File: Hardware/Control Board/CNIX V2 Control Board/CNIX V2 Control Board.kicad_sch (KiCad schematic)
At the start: 71 parts, among them J1 EXT, J10 LED, J11 USB_C_Receptacle, J3 Tube Out, J4 EXT, J5 I2C_ext, J6 Prog, J7 HT, J8 GND, J9 GND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

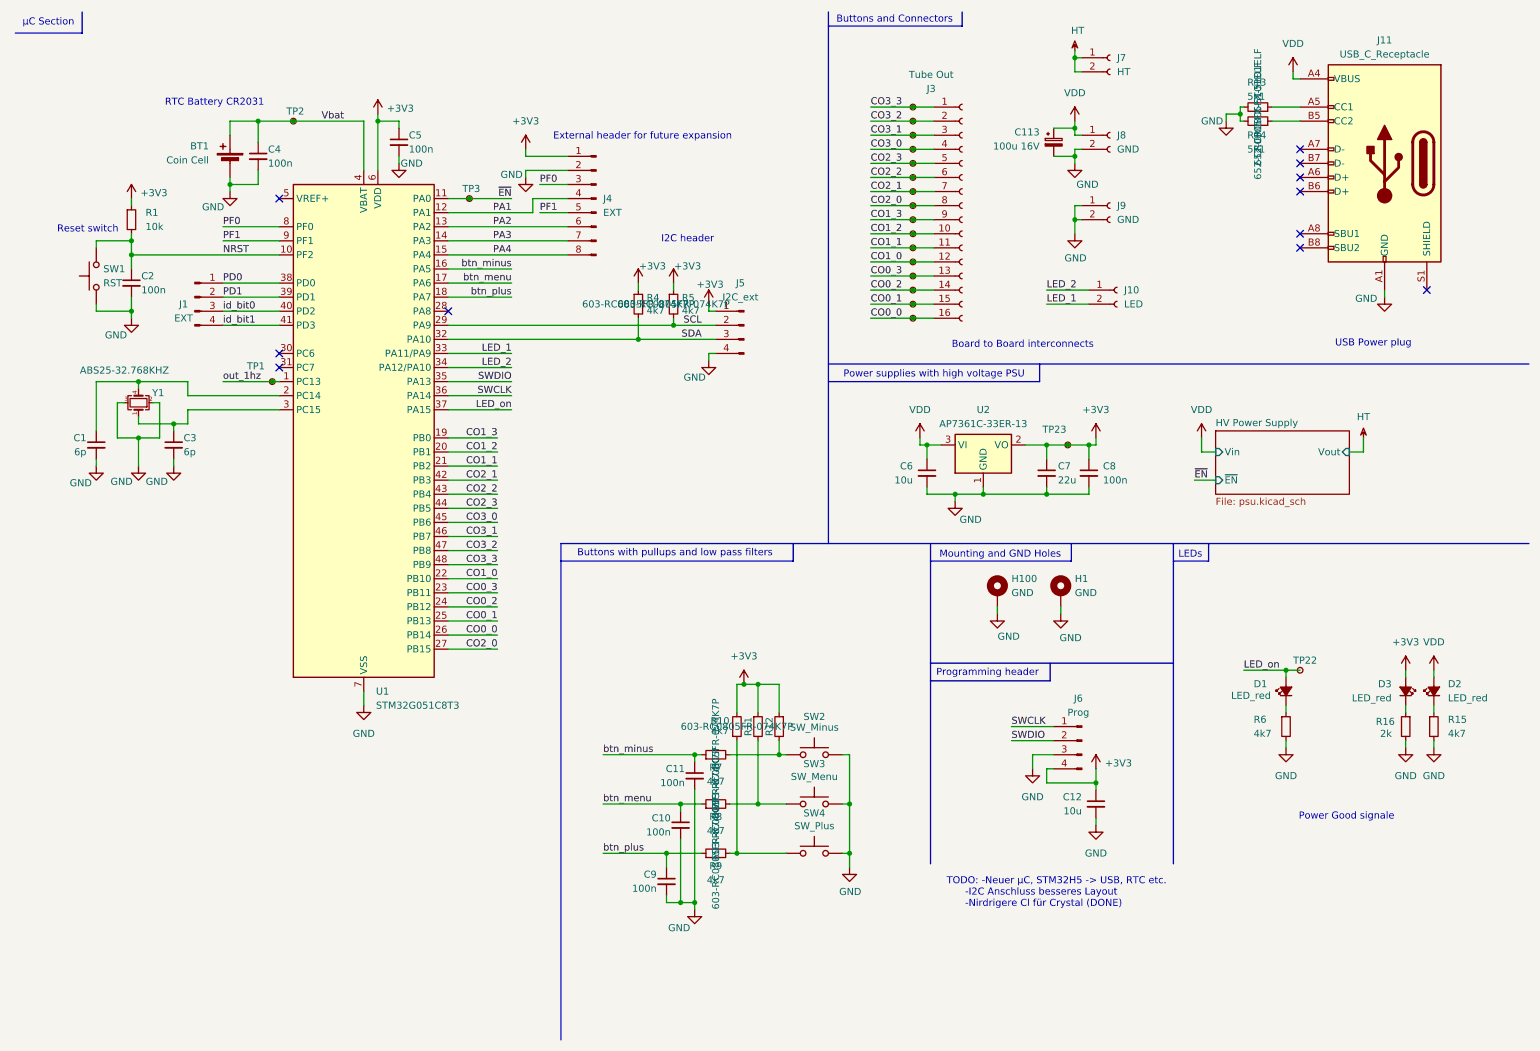
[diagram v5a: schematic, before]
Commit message: finalized V2 and cleaned up Silkscreen
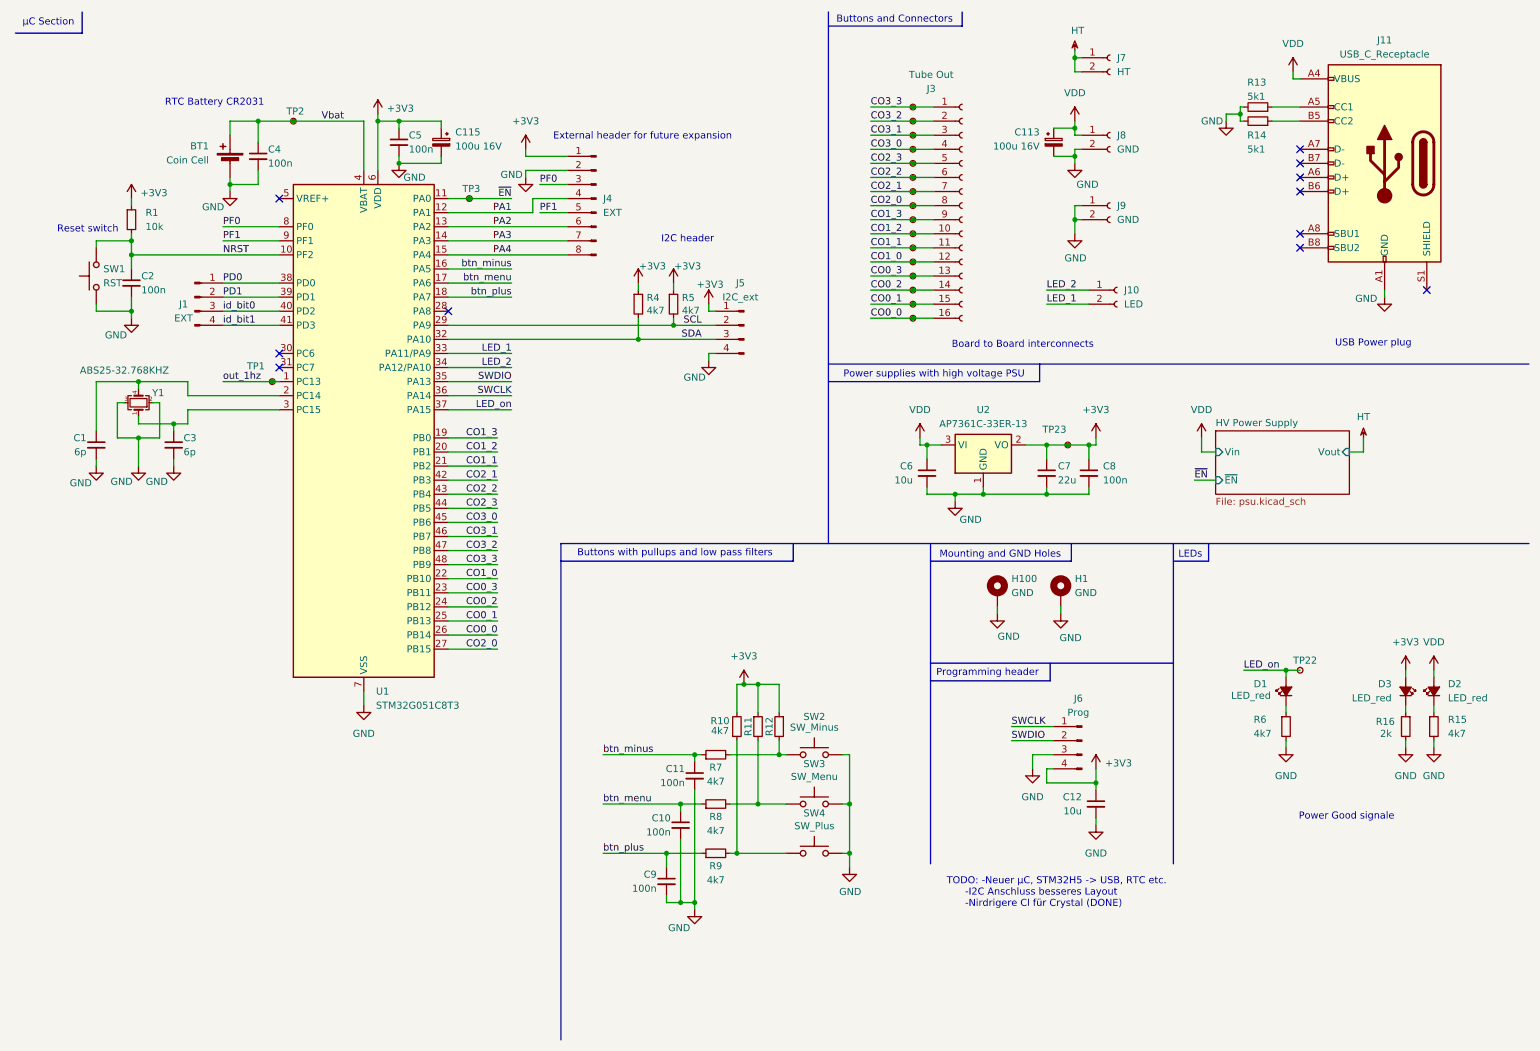
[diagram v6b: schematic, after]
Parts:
- added C115: 100u 16V, Capacitor_SMD:CP_Elec_6.3x7.7, symbol Device:C_Polarized_Small
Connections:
- net +3V3: now also C115.1
- net GND: now also C115.2
